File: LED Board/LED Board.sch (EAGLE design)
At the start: 3 parts

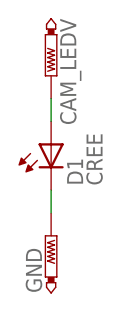
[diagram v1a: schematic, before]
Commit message: Added symbols to the LED board
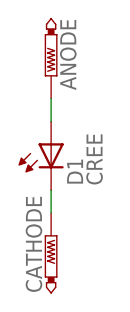
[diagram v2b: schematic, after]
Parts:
- renumbered CAM_LEDV to ANODE, GND to CATHODE
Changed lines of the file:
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@@
 <parts>
 <part name="D1" library="2015_LED_Driver" deviceset="CREE" device=""/>
-<part name="CAM_LEDV" library="testpad" deviceset="PTR1" device="PAD1-20"/>
-<part name="GND" library="testpad" deviceset="PTR1" device="PAD1-20"/>
+<part name="ANODE" library="testpad" deviceset="PTR1" device="PAD1-20"/>
+<part name="CATHODE" library="testpad" deviceset="PTR1" device="PAD1-20"/>
 </parts>
 <sheets>
@@
 <instances>
 <instance part="D1" gate="G$1" x="43.18" y="60.96"/>
-<instance part="CAM_LEDV" gate="G$1" x="43.18" y="68.58" rot="R180"/>
-<instance part="GND" gate="G$1" x="43.18" y="50.8"/>
+<instance part="ANODE" gate="G$1" x="43.18" y="68.58" rot="R180"/>
+<instance part="CATHODE" gate="G$1" x="43.18" y="50.8"/>
 </instances>
 <busses>
@@
 <segment>
 <pinref part="D1" gate="G$1" pin="A"/>
-<pinref part="CAM_LEDV" gate="G$1" pin="TP"/>
+<pinref part="ANODE" gate="G$1" pin="TP"/>
 <wire x1="43.18" y1="66.04" x2="43.18" y2="63.5" width="0.1524" layer="91"/>
 </segment>
@@
 <segment>
 <pinref part="D1" gate="G$1" pin="C"/>
-<pinref part="GND" gate="G$1" pin="TP"/>
+<pinref part="CATHODE" gate="G$1" pin="TP"/>
 <wire x1="43.18" y1="53.34" x2="43.18" y2="55.88" width="0.1524" layer="91"/>
 </segment>
